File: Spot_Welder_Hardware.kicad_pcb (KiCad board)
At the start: 2 copper layers, 256.5 x 182.9 mm, 155 parts, among them J1 Mini USB, J2 Conn_01x03_Male, Q1 Q_NMOS_GSD, Q10 Q_NMOS_GDS, Q11 Q_NMOS_GDS, Q12 Q_NMOS_GDS, Q13 Q_NMOS_GDS, Q2 MBT3904, Q3 Q_NMOS_GDS, Q4 Q_NMOS_GDS, Q5 Q_NMOS_GDS, Q6 Q_NMOS_GDS, Q7 Q_NMOS_GDS, Q8 Q_NMOS_GDS, Q9 Q_NMOS_GDS, SW1 SW_Push, SW2 SW_SPDT, SW3 Lead Voltage Trigger, SW4 SW_Push, U1 OKI, U2 ATMEGA328P, U3 FAN3122TMXCT-ND, U4 FT232RL, U5 FAN3122TMXCT-ND, Y1 Crystal

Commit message: Fixed outline and mounting holes
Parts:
- removed the REF** at (11.2, 190.8)
- removed the REF** at (22.4, 191.5)
- removed the REF** at (272.5, 16.3)
- added REF**: 6-32 Screw Hole, Project Library:6-32 Screw Hole, F.Cu at (10.2, 198.1)
- added REF**: 6-32 Screw Hole, Project Library:6-32 Screw Hole, F.Cu at (19.3, 18.8)
- added REF**: 6-32 Screw Hole, Project Library:6-32 Screw Hole, F.Cu at (275.8, 191.5)
- moved REF** 256.8 mm to (277.9, 18.5), turned to 270 degrees
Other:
- board size 256.5 x 182.9 mm -> 268.7 x 183.1 mm
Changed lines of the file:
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@@
     (mod_text_size 1 1)
     (mod_text_width 0.15)
-    (pad_size 18.288 18.288)
-    (pad_drill 9.144)
+    (pad_size 3.683 3.683)
+    (pad_drill 0.762)
     (pad_to_mask_clearance 0.2)
     (aux_axis_origin 0 0)
@@
     (add_net V_Sense)
   )
+  (module "Project Library:6-32 Screw Hole" (layer F.Cu)
+    (at 10.16 198.12 90)
+    (fp_text reference REF** (at 0 0.5 90) (layer F.SilkS) hide
+      (effects (font (size 1 1) (thickness 0.15)))
+    )
+    (fp_text value "6-32 Screw Hole" (at 0 -0.5 90) (layer F.Fab)
+      (effects (font (size 1 1) (thickness 0.15)))
+    )
+    (pad "" np_thru_hole circle (at 6.604 9.144 90) (size 3.683 3.683) (drill 0.762) (layers *.Cu *.Mask))
+  )
+  (module "Project Library:6-32 Screw Hole" (layer F.Cu)
+    (at 19.304 18.796)
+    (fp_text reference REF** (at 0 0.5) (layer F.SilkS) hide
+      (effects (font (size 1 1) (thickness 0.15)))
+    )
+    (fp_text value "6-32 Screw Hole" (at 0 -0.5) (layer F.Fab)
+      (effects (font (size 1 1) (thickness 0.15)))
+    )
+    (pad "" np_thru_hole circle (at 0 0) (size 3.683 3.683) (drill 0.762) (layers *.Cu *.Mask))
+  )
+  (module "Project Library:6-32 Screw Hole" (layer F.Cu)
+    (at 275.844 191.516 180)
+    (fp_text reference REF** (at 0 0.5 180) (layer F.SilkS) hide
+      (effects (font (size 1 1) (thickness 0.15)))
+    )
+    (fp_text value "6-32 Screw Hole" (at 0 -0.5 180) (layer F.Fab)
+      (effects (font (size 1 1) (thickness 0.15)))
+    )
+    (pad "" np_thru_hole circle (at -2.032 0 180) (size 3.683 3.683) (drill 0.762) (layers *.Cu *.Mask))
+  )
   (module Resistors_SMD:R_0603_HandSoldering (layer F.Cu)
     (at 46.693 145.923 180)
@@
       (net 4 GND))
   )
-  (module "Project Library:6-32 Screw Hole" (layer F.Cu)
-    (at 11.176 190.754)
-    (fp_text reference REF** (at 0 0.5) (layer F.SilkS) hide
-      (effects (font (size 1 1) (thickness 0.15)))
-    )
-    (fp_text value "6-32 Screw Hole" (at 0 -0.5) (layer F.Fab)
-      (effects (font (size 1 1) (thickness 0.15)))
-    )
-    (pad "" np_thru_hole circle (at 261.366 0.762) (size 3.683 3.683) (drill 0.762) (layers *.Cu *.Mask))
-  )
-  (module "Project Library:6-32 Screw Hole" (layer F.Cu)
-    (at 22.352 191.516)
-    (fp_text reference REF** (at 0 0.5) (layer F.SilkS) hide
-      (effects (font (size 1 1) (thickness 0.15)))
-    )
-    (fp_text value "6-32 Screw Hole" (at 0 -0.5) (layer F.Fab)
-      (effects (font (size 1 1) (thickness 0.15)))
-    )
-    (pad "" np_thru_hole circle (at -1.27 0) (size 3.683 3.683) (drill 0.762) (layers *.Cu *.Mask))
-  )
-  (module "Project Library:6-32 Screw Hole" (layer F.Cu)
-    (at 272.542 16.256)
-    (fp_text reference REF** (at 0 0.5) (layer F.SilkS) hide
-      (effects (font (size 1 1) (thickness 0.15)))
-    )
-    (fp_text value "6-32 Screw Hole" (at 0 -0.5) (layer F.Fab)
-      (effects (font (size 1 1) (thickness 0.15)))
-    )
-    (pad "" np_thru_hole circle (at 0 0) (size 3.683 3.683) (drill 0.762) (layers *.Cu *.Mask))
-  )
   (module MRDT_Devices:BUZZER_SMI_1324_TW_5V_2_R (layer F.Cu)
     (at 145.542 145.256 270)
@@
   )
   (module "Project Library:6-32 Screw Hole" (layer F.Cu)
-    (at 21.082 16.256)
-    (fp_text reference REF** (at 0 0.5) (layer F.SilkS) hide
+    (at 277.876 18.542 270)
+    (fp_text reference REF** (at 0 0.5 270) (layer F.SilkS) hide
       (effects (font (size 1 1) (thickness 0.15)))
     )
-    (fp_text value "6-32 Screw Hole" (at 0 -0.5) (layer F.Fab)
+    (fp_text value "6-32 Screw Hole" (at 0 -0.5 270) (layer F.Fab)
       (effects (font (size 1 1) (thickness 0.15)))
     )
-    (pad "" np_thru_hole circle (at 0 0) (size 3.683 3.683) (drill 0.762) (layers *.Cu *.Mask))
+    (pad "" np_thru_hole circle (at 0 0 270) (size 3.683 3.683) (drill 0.762) (layers *.Cu *.Mask))
   )
   (module "Project Library:Lead Connection" (layer F.Cu)
@@
       (xy 3.076472 -5.52068) (xy 3.111284 -5.541334) (xy 3.12377 -5.541189)) (layer F.SilkS) (width 0.01))
   )
+  (gr_line (start 14.224 18.796) (end 14.224 191.516) (layer Edge.Cuts) (width 0.15))
+  (gr_line (start 19.304 196.596) (end 277.876 196.596) (layer Edge.Cuts) (width 0.15))
+  (gr_arc (start 19.304 191.516) (end 14.224 191.516) (angle -90) (layer Edge.Cuts) (width 0.15))
+  (gr_circle (center 19.304 191.516) (end 14.224 191.516) (layer F.SilkS) (width 0.2))
+  (gr_line (start 277.876 13.462) (end 19.304 13.716) (layer Edge.Cuts) (width 0.15))
+  (gr_circle (center 19.304 18.796) (end 19.304 13.716) (layer F.SilkS) (width 0.2))
+  (gr_arc (start 19.304 18.796) (end 19.304 13.716) (angle -90) (layer Edge.Cuts) (width 0.15))
+  (gr_line (start 282.956 191.516) (end 282.956 18.542) (layer Edge.Cuts) (width 0.15))
+  (gr_circle (center 277.876 191.516) (end 277.876 196.596) (layer F.SilkS) (width 0.2))
+  (gr_arc (start 277.876 191.516) (end 277.876 196.596) (angle -90) (layer Edge.Cuts) (width 0.15))
+  (gr_circle (center 277.876 18.542) (end 282.956 18.542) (layer F.SilkS) (width 0.2))
+  (gr_arc (start 277.876 18.542) (end 282.956 18.542) (angle -90) (layer Edge.Cuts) (width 0.15))
   (gr_text DTR (at 71.628 188.976) (layer F.SilkS)
     (effects (font (size 1.5 1.5) (thickness 0.3)))
@@
     (effects (font (size 2.54 2.54) (thickness 0.508)) (justify left))
   )
-  (gr_line (start 18.542 14.732) (end 18.542 18.796) (layer Edge.Cuts) (width 0.15))
-  (gr_line (start 23.622 13.716) (end 19.558 13.716) (layer Edge.Cuts) (width 0.15))
-  (gr_arc (start 19.558 14.732) (end 19.558 13.716) (angle -90) (layer Edge.Cuts) (width 0.15))
-  (gr_line (start 274.066 13.716) (end 270.002 13.716) (layer Edge.Cuts) (width 0.15))
-  (gr_line (start 275.082 18.796) (end 275.082 14.732) (layer Edge.Cuts) (width 0.15))
-  (gr_arc (start 274.066 14.732) (end 275.082 14.732) (angle -90) (layer Edge.Cuts) (width 0.15))
-  (gr_line (start 270.002 196.596) (end 23.622 196.596) (layer Edge.Cuts) (width 0.15))
-  (gr_line (start 275.082 191.516) (end 275.082 18.796) (layer Edge.Cuts) (width 0.15))
-  (gr_line (start 270.002 13.716) (end 23.622 13.716) (layer Edge.Cuts) (width 0.15))
-  (gr_arc (start 270.002 191.516) (end 270.002 196.596) (angle -90) (layer Edge.Cuts) (width 0.15))
-  (gr_arc (start 23.622 191.516) (end 18.542 191.516) (angle -90) (layer Edge.Cuts) (width 0.15))
-  (gr_line (start 18.542 191.516) (end 18.542 18.796) (layer Edge.Cuts) (width 0.15))
   (gr_line (start -91.44 254) (end -91.44 -254) (layer F.SilkS) (width 0.2))
   (segment (start 68.326 148.336) (end 67.691 147.701) (width 0.381) (layer F.Cu) (net 1))
@@
         (xy 223.52 196.596) (xy 223.52 154.94) (xy 178.054 154.94) (xy 178.054 196.596) (xy 146.812 196.596)
         (xy 146.812 139.446) (xy 86.106 139.446) (xy 86.106 108.712) (xy 53.848 108.712) (xy 53.848 182.372)
-        (xy 18.542 182.372) (xy 18.542 13.716) (xy 275.082 13.716) (xy 275.082 196.596)
+        (xy 14.224 182.372) (xy 14.224 13.716) (xy 282.956 13.716) (xy 282.956 196.596)
       )
     )
@@
       (pts
         (xy 146.304 196.596) (xy 146.304 139.954) (xy 86.106 139.954) (xy 86.106 145.796) (xy 54.356 145.796)
-        (xy 54.356 182.88) (xy 18.542 182.88) (xy 18.542 196.596) (xy 137.414 196.596)
+        (xy 54.356 182.88) (xy 14.224 182.88) (xy 14.224 196.596) (xy 137.414 196.596)
       )
     )
@@
     (polygon
       (pts
-        (xy 18.542 182.118) (xy 53.848 182.118) (xy 53.848 132.842) (xy 18.542 132.842)
+        (xy 14.224 182.372) (xy 53.848 182.372) (xy 53.848 132.842) (xy 14.224 132.842)
       )
     )
@@
     (polygon
       (pts
-        (xy 54.356 139.446) (xy 146.812 139.446) (xy 146.812 196.596) (xy 275.082 196.596) (xy 275.082 13.716)
-        (xy 18.542 13.716) (xy 18.542 132.08) (xy 54.356 132.334)
+        (xy 54.356 139.446) (xy 146.812 139.446) (xy 146.812 196.596) (xy 282.956 196.596) (xy 282.956 13.716)
+        (xy 14.224 13.716) (xy 14.224 132.334) (xy 54.356 132.334)
       )
     )
@@
     (polygon
       (pts
-        (xy 18.542 182.88) (xy 54.356 182.88) (xy 54.356 139.954) (xy 146.304 139.954) (xy 146.304 196.596)
-        (xy 18.542 196.596)
+        (xy 14.224 182.88) (xy 54.356 182.88) (xy 54.356 139.954) (xy 146.304 139.954) (xy 146.304 196.596)
+        (xy 14.224 196.596)
       )
     )

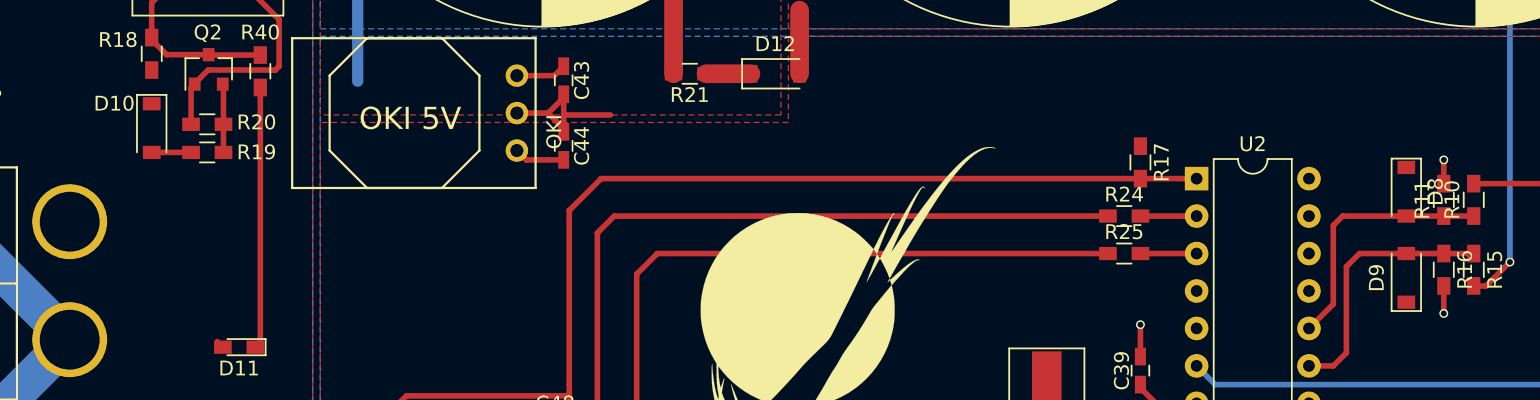
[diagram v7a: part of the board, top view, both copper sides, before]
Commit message: Replaced D8, D9 with Shottky Diode
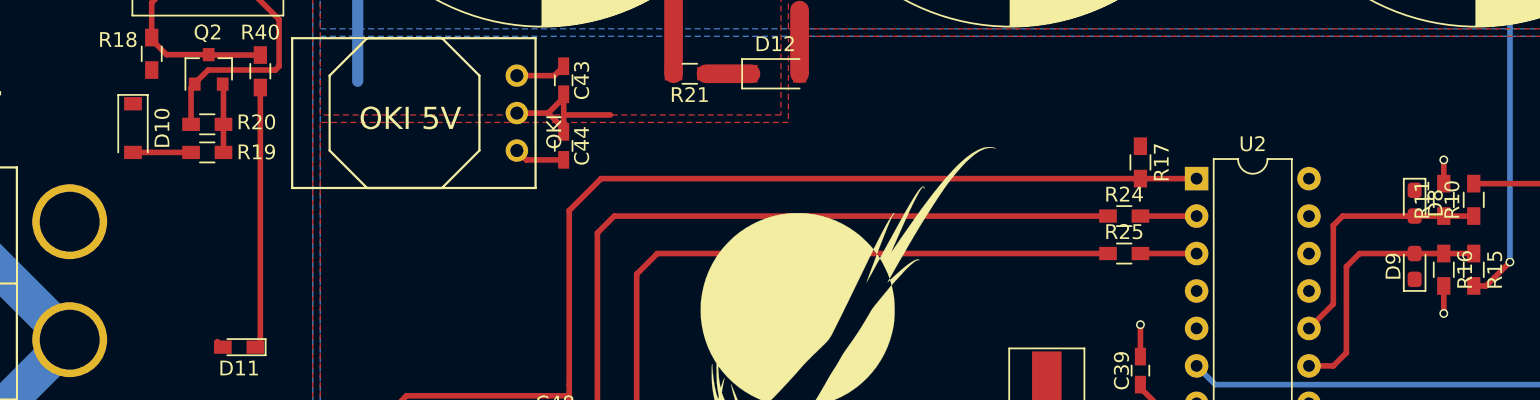
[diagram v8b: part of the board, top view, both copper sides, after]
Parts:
- D8, D9: value 5V -> D_Schottky; footprint Diodes_SMD:D_SOD-123 -> Diode_SMD:D_0603_1608Metric_Pad1.05x0.95mm_HandSolder
- moved D10 1.27 mm to (41.7, 146.2)
- moved D9 0.96 mm to (128.6, 155.6)
- moved D8 0.96 mm to (128.6, 151.3)
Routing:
- net Net-(D10-Pad2): track 2.84 -> 4.11 mm
